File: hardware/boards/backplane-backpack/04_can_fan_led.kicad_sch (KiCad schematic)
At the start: 25 parts, among them J2 GND/CANL/CANH (TBD), J9 12V FAN, Q1 AO3407A, Q2 2N7002,215, U3 TCAN3413DR

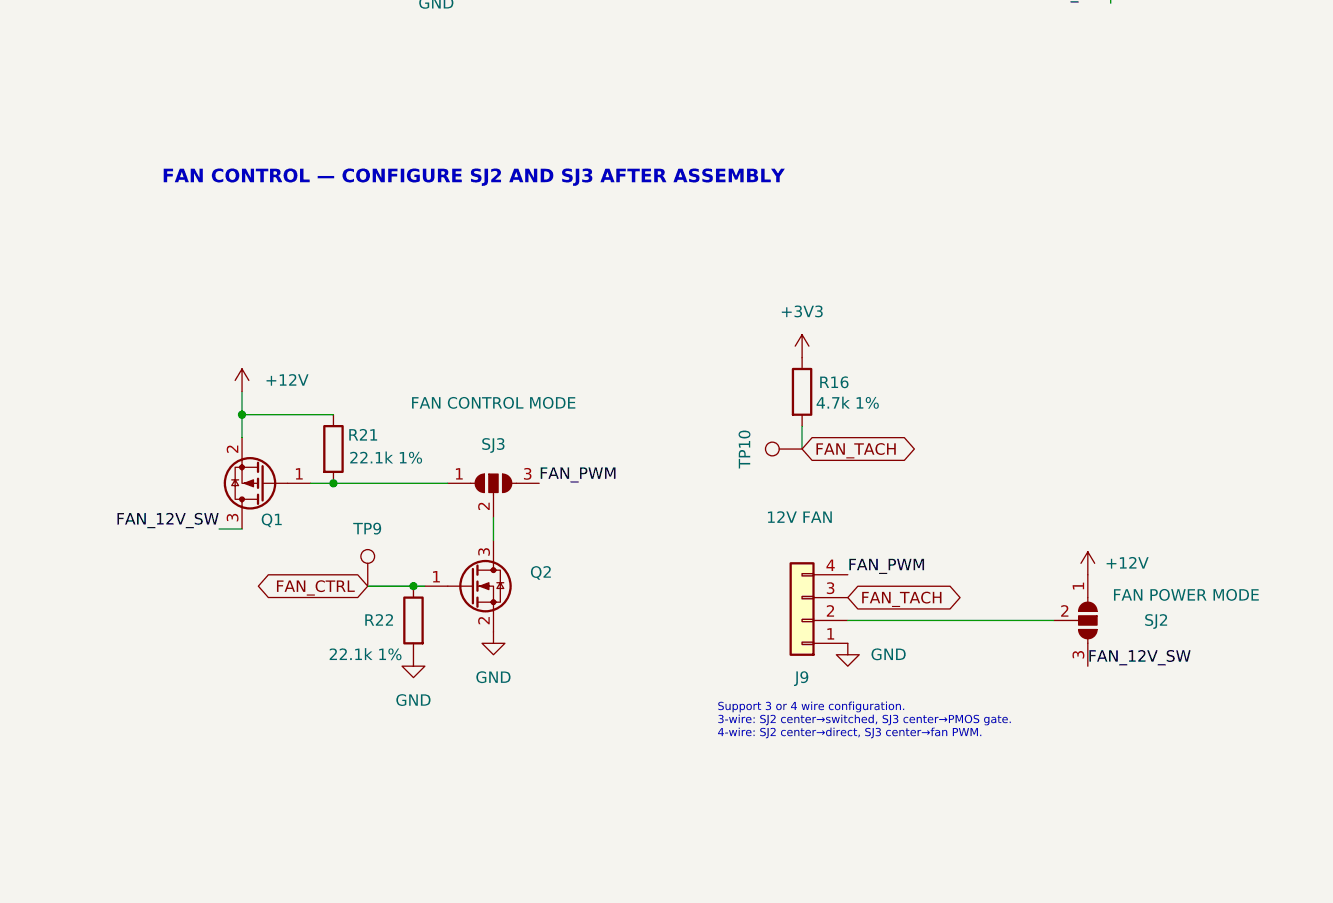
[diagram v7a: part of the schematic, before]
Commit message: hardware: simplify backpack fan interface
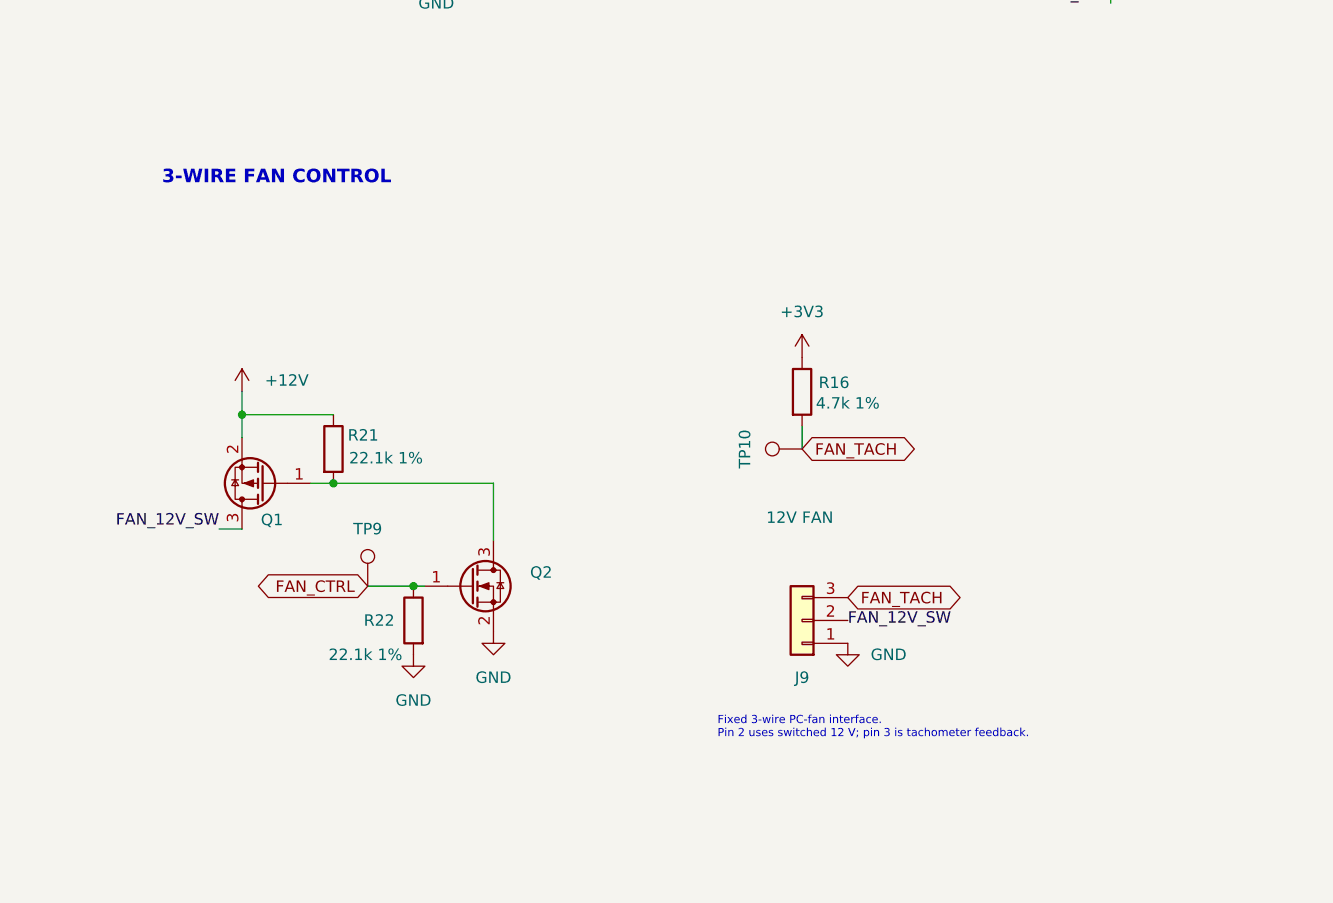
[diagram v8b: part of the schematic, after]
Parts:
- removed SJ2: FAN POWER MODE, Jumper:SolderJumper-3_P1.3mm_Open_Pad1.0x1.5mm, symbol Jumper:SolderJumper_3_Open
- removed SJ3: FAN CONTROL MODE, Jumper:SolderJumper-3_P1.3mm_Open_Pad1.0x1.5mm, symbol Jumper:SolderJumper_3_Open
- J9: footprint (none) -> Connector:FanPinHeader_1x03_P2.54mm_Vertical; symbol Connector_Generic:Conn_01x04 -> Connector_Generic:Conn_01x03; Package TBD -> 3-pin 2.54 mm PC-fan header; Population TBD -> POP
- Q1: Population POP/DNP -> POP
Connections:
- net FAN_12V_SW: now also J9.2 (Pin_2)
- net at Q1.1 (G), R21.2: now also Q2.3 (D)
- removed net FAN_PWM: J9.4 (Pin_4)
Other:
- note added: "3-WIRE FAN CONTROL"
- note added: "Fixed 3-wire PC-fan interface. Pin 2 uses switched 12 V; pin 3 is tachometer feedback."
- note removed: "FAN CONTROL — CONFIGURE SJ2 AND SJ3 AFTER ASSEMBLY"
- note removed: "Support 3 or 4 wire configuration. 3-wire: SJ2 center→switched, SJ3 center→PMOS gate. 4-wire: SJ2 center→direct, SJ3 center→fan PWM."
